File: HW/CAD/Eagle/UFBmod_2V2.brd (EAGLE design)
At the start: 98.4 x 89.5 mm, 204 parts, among them J1411 ABRACON_ARJE-0034, T0551 MMBT2222, U0501 MIDAS_MCCOG21605B6W-FPTLWI, U0601 MAX5217, U0701 AT86RF215-ZU, U0711 ASVTX-13-D-26.000MHZ-I05-T, U0811 PE4259, U0821 RFX1010, U0881 B39871B3440U410, U0911 FT232HL, U1101 TPS53353, U1211 TPS62745DSSR, X0891 ANTENNATINY, X0895 ANTENNATINY, X1011 TTE_EN11-HSM, X1311 MOLEX 105017-0001, X1351 PHOENIX_1990067_1X8X2MM50_PTS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, X1361 PHOENIX_1990067_1X8X2MM50_PTS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

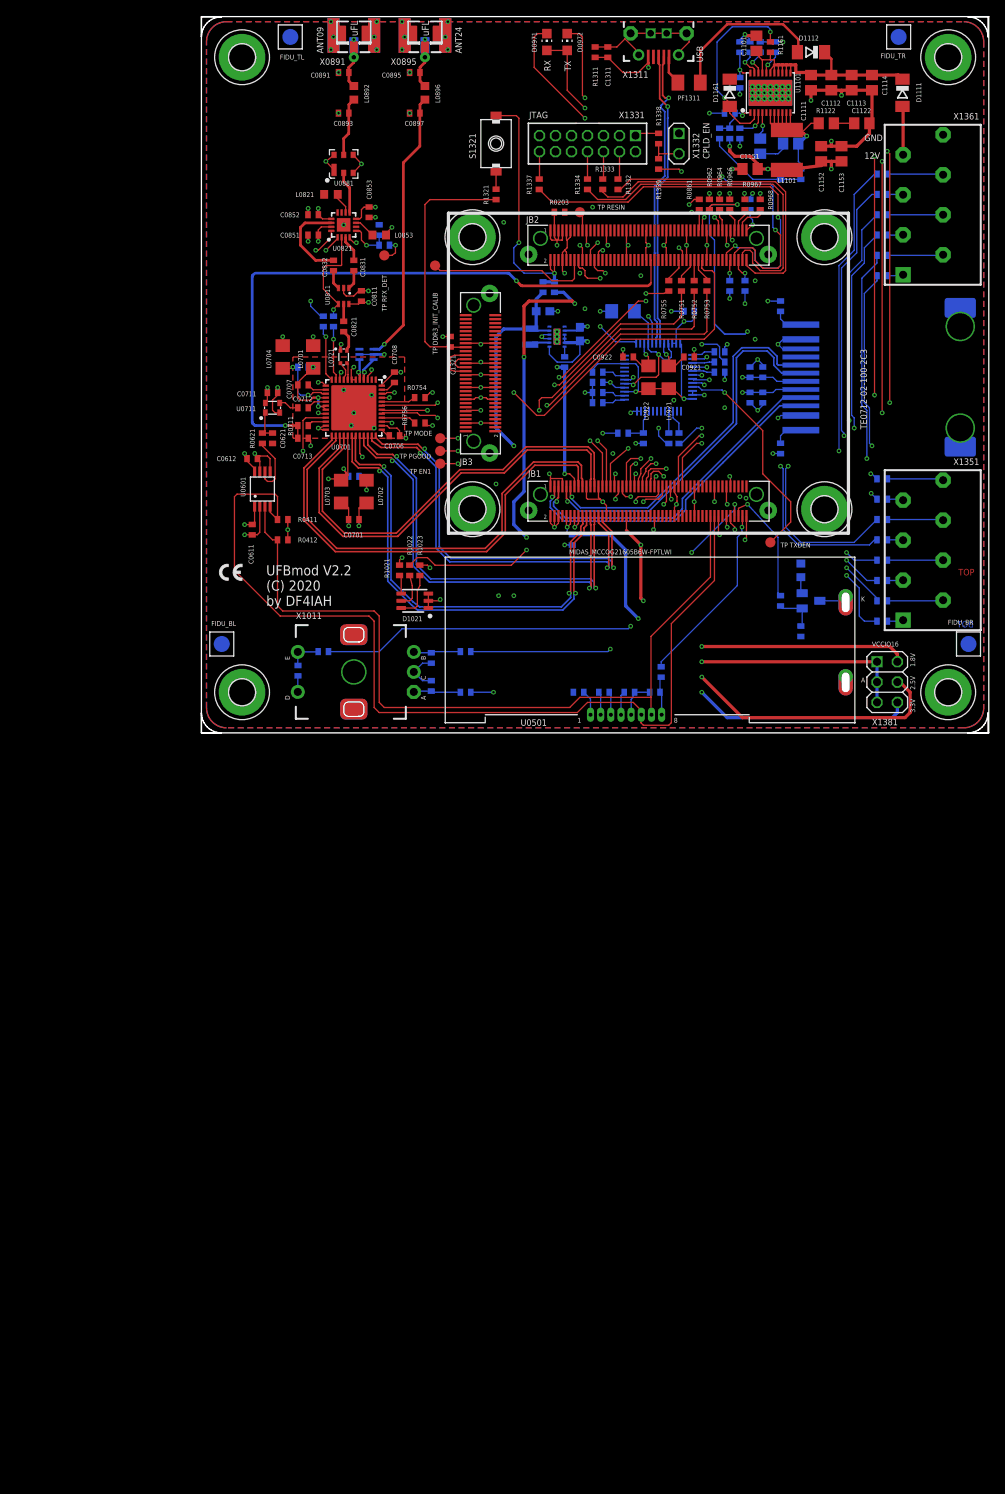
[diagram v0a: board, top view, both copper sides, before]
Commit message: HW - Eagle - V2.2 - FT232H supply fixes, suppressor diodes to be added, layout still to do.
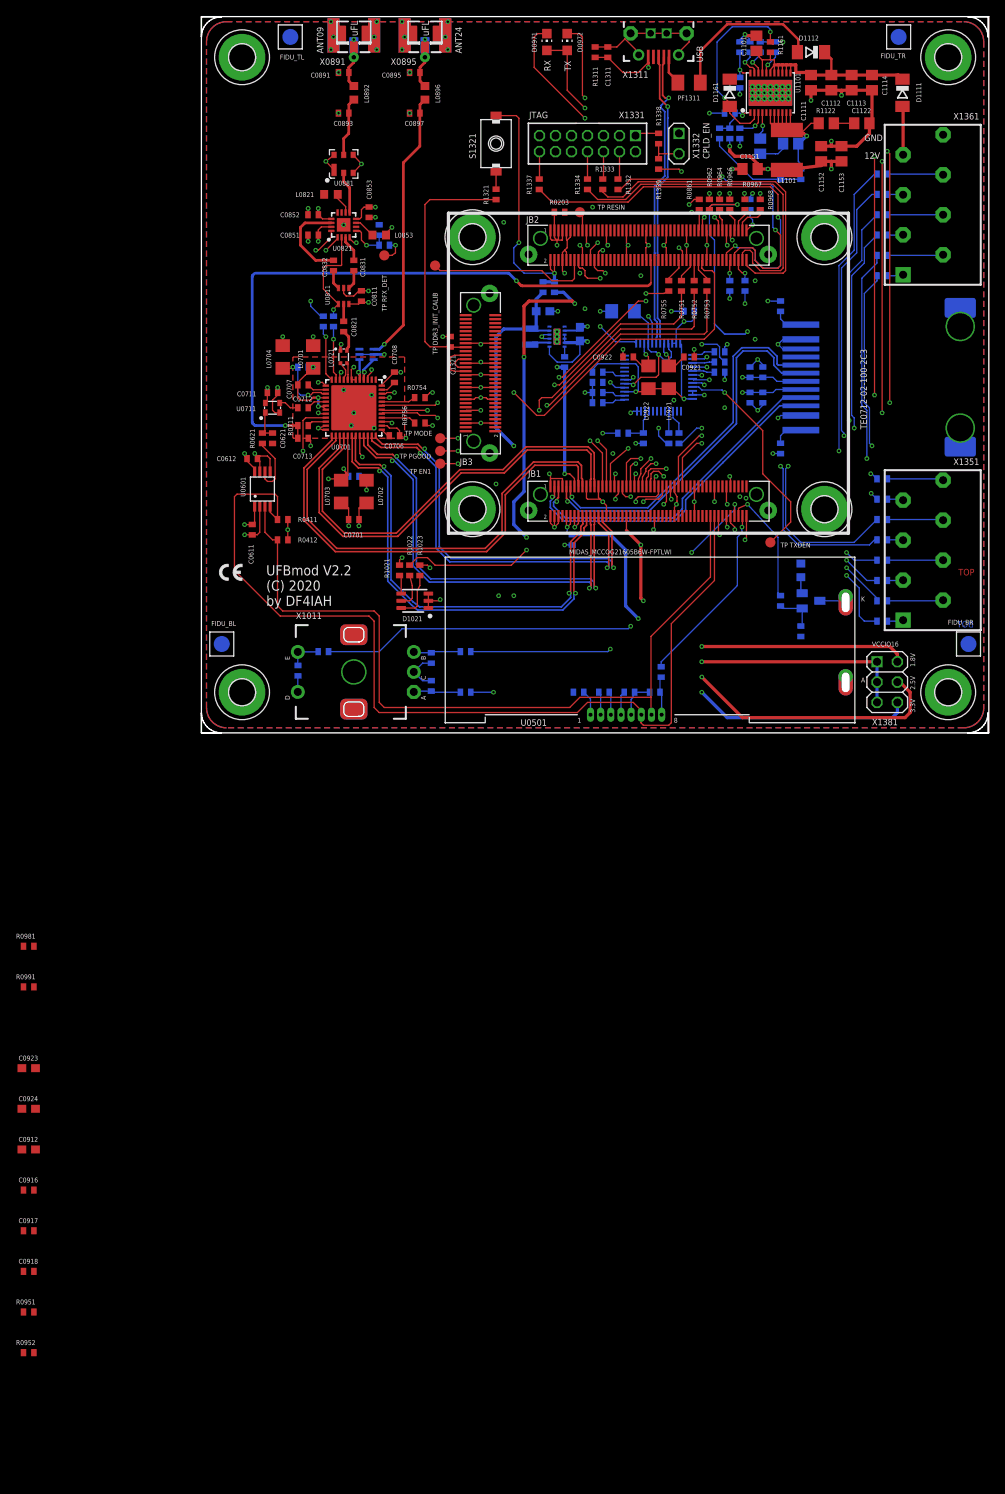
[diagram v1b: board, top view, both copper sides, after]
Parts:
- added C0914, C0916, C0917, C0918: 100nF, df4iah_rcl:C0402
- added C0923, C0924: 4.7uF, df4iah_rcl:C0603
- added R0951, R0952: 0R, df4iah_rcl:R0402
- added R0981: 10kR, df4iah_rcl:R0402
- added R0991: N/A, df4iah_rcl:R0402
- C0912: value 100nF -> 4.7uF; device df4iah_rcl:C0402 -> df4iah_rcl:C0603
- moved C0912 118.4 mm to (-21.6, -52.1), flipped to the top, turned to 0 degrees
- moved C0913 1.27 mm to (49.5, 42.5)
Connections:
- net PMIC3V3_SW renamed PMIC2V5_SW
- removed net FT_VCCCORE: C0912.2, U0911.38
- removed net FT_VCCD: D0971.A, D0972.A, L0921.2, L0922.2, R0931.2, U0911.12, U0911.24, U0911.39, U0911.46
- new net FT_ACBUS7: R0991.2, U0911.31
- new net FT_VCORE: C0913.2, U0911.38
- new net N$1: R0951.2, U0911.6
- new net N$3: R0952.2, U0911.7
- net +3V3: now also C0912.1, C0916.1, C0917.1, C0918.1, D0971.A, D0972.A, L0921.2, L0922.2, R0931.2, R0981.2, U0911.12, U0911.24, U0911.39, U0911.46
- net +5V_USB: now also R0991.1
- net FT_TXDEN: now also R0981.1
- net FT_VCCA: now also C0914.2; no longer C0913.2
- net FT_VPHY: now also C0924.1
- net FT_VPLL: now also C0923.1
- net GND: now also C0912.2, C0914.1, C0916.2, C0917.2, C0918.2, C0923.2, C0924.2; no longer C0912.1
- net USB_D_N: now also R0951.1; no longer U0911.6
- net USB_D_P: now also R0952.1; no longer U0911.7
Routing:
- net FT_VCCD: track 130.4 -> 0.00 mm, vias 5 -> 0
- net +3V3: track 124.7 -> 254.2 mm, vias 22 -> 27
- net FT_VCORE: track 0.00 -> 2.91 mm
- net FT_VCCCORE: track 2.91 -> 0.00 mm
- net USB_D_P: track 36.9 -> 36.1 mm
- net USB_D_N: track 37.7 -> 37.0 mm

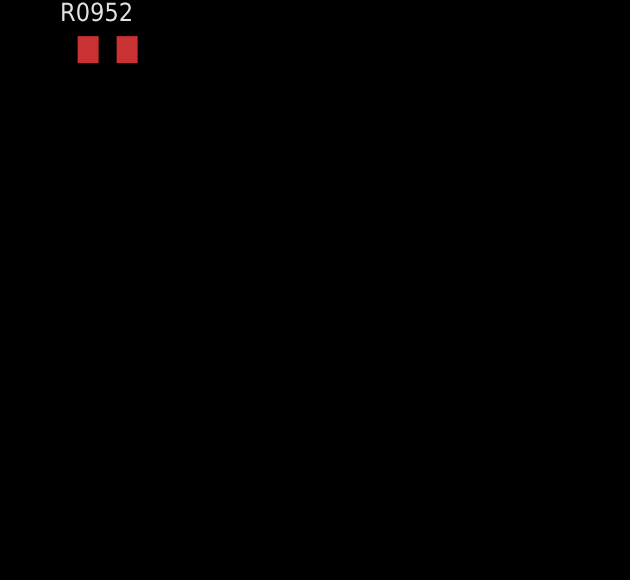
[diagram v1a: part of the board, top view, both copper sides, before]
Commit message: HW - Eagle - V2.2 - font size changed for DAC and volt. reference
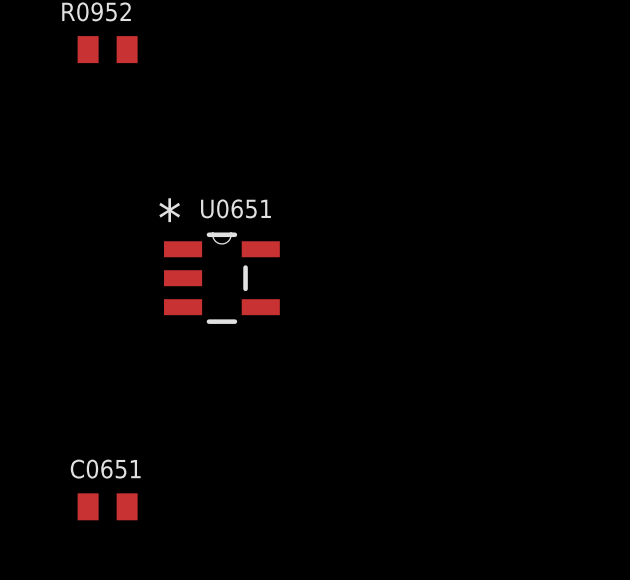
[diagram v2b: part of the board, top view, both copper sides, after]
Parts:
- added C0651: 100nF, df4iah_rcl:C0402
- added U0651: LM4120IM5-3.0, df4iah_powersupply:SOT95P285X120-5N
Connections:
- new net +3V0_20MHZ_VCTCXO: C0611.1, U0601.1, U0651.5
- net +3V3: now also C0651.1, U0651.3, U0651.4; no longer C0611.1, U0601.1
- net GND: now also C0651.2, U0651.2
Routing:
- net +3V3: track 254.2 -> 250.8 mm, vias 27 -> 26
- net +3V0_20MHZ_VCTCXO: track 0.00 -> 3.36 mm, vias 0 -> 1
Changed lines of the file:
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@@
 <element name="R0951" library="df4iah_rcl" package="R0402" value="0R" x="-21.59" y="-72.39"/>
 <element name="R0952" library="df4iah_rcl" package="R0402" value="0R" x="-21.59" y="-77.47"/>
+<element name="U0651" library="df4iah_powersupply" package="SOT95P285X120-5N" value="LM4120IM5-3.0" x="-17.78" y="-85.09">
+<attribute name="OC_FARNELL" value="1312745" x="-17.78" y="-85.09" size="1.778" layer="27" display="off"/>
+<attribute name="MPN" value="LM4120IM5-3.0" x="-17.78" y="-85.09" size="1.778" layer="27" display="off"/>
+<attribute name="OC_NEWARK" value="41K5441" x="-17.78" y="-85.09" size="1.778" layer="27" display="off"/>
+<attribute name="PACKAGE" value="SOT-23-5" x="-17.78" y="-85.09" size="1.778" layer="27" display="off"/>
+<attribute name="SUPPLIER" value="National Semiconductors" x="-17.78" y="-85.09" size="1.778" layer="27" display="off"/>
+</element>
+<element name="C0651" library="df4iah_rcl" package="C0402" value="100nF" x="-21.59" y="-92.71"/>
 </elements>
 <signals>
@@
 <contactref element="C0917" pad="2"/>
 <contactref element="C0918" pad="2"/>
+<contactref element="U0651" pad="2"/>
+<contactref element="C0651" pad="2"/>
 <wire x1="92.71" y1="74.77" x2="93.345" y2="84.455" width="0" layer="19" extent="1-1"/>
 <wire x1="83.82" y1="76.2" x2="92.71" y2="74.77" width="0" layer="19" extent="1-1"/>
@@
 <wire x1="-20.94" y1="-62.23" x2="-20.94" y2="-57.15" width="0" layer="19" extent="1-1"/>
 <wire x1="-20.94" y1="-67.31" x2="-20.94" y2="-62.23" width="0" layer="19" extent="1-1"/>
+<wire x1="-19.0754" y1="-85.09" x2="-20.94" y2="-67.31" width="0" layer="19" extent="1-1"/>
+<wire x1="-20.94" y1="-92.71" x2="-19.0754" y2="-85.09" width="0" layer="19" extent="1-1"/>
 </signal>
 <signal name="+3V3">
@@
 <contactref element="U0821" pad="15"/>
 <contactref element="C0612" pad="1"/>
-<contactref element="C0611" pad="1"/>
-<contactref element="U0601" pad="1"/>
 <wire x1="18.4" y1="26.67" x2="18.4" y2="28.1205" width="0.1524" layer="1"/>
 <wire x1="18.4" y1="28.1205" x2="17.4625" y2="28.7405" width="0.1524" layer="1"/>
@@
 <wire x1="10.795" y1="25.4" x2="10.795" y2="24.145" width="0.1524" layer="1"/>
 <wire x1="10.795" y1="24.145" x2="10.81" y2="24.13" width="0.1524" layer="1"/>
-<via x="5.3975" y="26.035" extent="1-16" drill="0.3"/>
-<wire x1="5.3975" y1="26.035" x2="6.335" y2="26.035" width="0.1524" layer="1"/>
-<wire x1="6.335" y1="26.035" x2="6.35" y2="26.05" width="0.1524" layer="1"/>
-<wire x1="6.645" y1="28.33" x2="6.645" y2="26.345" width="0.1524" layer="1"/>
-<wire x1="6.645" y1="26.345" x2="6.35" y2="26.05" width="0.1524" layer="1"/>
 <wire x1="7.295" y1="32.63" x2="7.3025" y2="32.6375" width="0.1524" layer="1"/>
 <wire x1="7.3025" y1="32.6375" x2="7.3025" y2="33.9725" width="0.1524" layer="1"/>
@@
 <wire x1="71.4375" y1="41.5925" x2="60.4825" y2="41.5925" width="0.1524" layer="3"/>
 <wire x1="60.4825" y1="41.5925" x2="60.325" y2="41.75" width="0.1524" layer="3"/>
+<contactref element="U0651" pad="4"/>
+<contactref element="C0651" pad="1"/>
+<contactref element="U0651" pad="3"/>
 <wire x1="66.04" y1="74.28" x2="67.31" y2="79.8195" width="0" layer="19" extent="16-16"/>
 <wire x1="64.77" y1="72.0725" x2="66.04" y2="72.7075" width="0" layer="19" extent="1-3"/>
@@
 <wire x1="8.255" y1="43.18" x2="10.16" y2="48.412" width="0" layer="19" extent="1-1"/>
 <wire x1="6.6975" y1="34.925" x2="7.99" y2="41.24" width="0" layer="19" extent="1-1"/>
-<wire x1="6.645" y1="28.33" x2="7.295" y2="32.63" width="0" layer="19" extent="1-1"/>
-<wire x1="10.795" y1="26.655" x2="6.645" y2="26.345" width="0" layer="19" extent="1-1"/>
+<wire x1="10.81" y1="26.67" x2="8.595" y2="32.63" width="0" layer="19" extent="1-1"/>
 <wire x1="17.4625" y1="28.7405" x2="10.81" y2="26.67" width="0" layer="19" extent="1-1"/>
 <wire x1="52.84875" y1="5.08" x2="46.6725" y2="25.7175" width="0" layer="19" extent="16-16"/>
 <wire x1="80.53" y1="5.57" x2="52.84875" y2="5.08" width="0" layer="19" extent="1-16"/>
-<wire x1="-20.94" y1="-26.67" x2="5.3975" y2="26.035" width="0" layer="19" extent="1-1"/>
+<wire x1="-20.94" y1="-26.67" x2="10.795" y2="24.145" width="0" layer="19" extent="1-1"/>
 <wire x1="-22.44" y1="-52.07" x2="-20.94" y2="-26.67" width="0" layer="19" extent="1-1"/>
 <wire x1="-22.24" y1="-57.15" x2="-22.44" y2="-52.07" width="0" layer="19" extent="1-1"/>
 <wire x1="-22.24" y1="-62.23" x2="-22.24" y2="-57.15" width="0" layer="19" extent="1-1"/>
 <wire x1="-22.24" y1="-67.31" x2="-22.24" y2="-62.23" width="0" layer="19" extent="1-1"/>
+<wire x1="-19.0754" y1="-86.0552" x2="-22.24" y2="-67.31" width="0" layer="19" extent="1-1"/>
+<wire x1="-16.4846" y1="-86.0552" x2="-19.0754" y2="-86.0552" width="0" layer="19" extent="1-1"/>
+<wire x1="-22.24" y1="-92.71" x2="-19.0754" y2="-86.0552" width="0" layer="19" extent="1-1"/>
 </signal>
 <signal name="P$8">
@@
 <wire x1="-20.94" y1="-77.47" x2="57.35" y2="48.7" width="0" layer="19" extent="1-16"/>
 </signal>
+<signal name="+3V0_20MHZ_VCTCXO">
+<contactref element="U0651" pad="5"/>
+<contactref element="C0611" pad="1"/>
+<contactref element="U0601" pad="1"/>
+<via x="5.3975" y="26.035" extent="1-16" drill="0.3"/>
+<wire x1="5.3975" y1="26.035" x2="6.335" y2="26.035" width="0.1524" layer="1"/>
+<wire x1="6.335" y1="26.035" x2="6.35" y2="26.05" width="0.1524" layer="1"/>
+<wire x1="6.645" y1="28.33" x2="6.645" y2="26.345" width="0.1524" layer="1"/>
+<wire x1="6.645" y1="26.345" x2="6.35" y2="26.05" width="0.1524" layer="1"/>
+<wire x1="5.3975" y1="26.035" x2="-16.4846" y2="-84.1248" width="0" layer="19" extent="1-1"/>
+</signal>
 </signals>

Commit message: HW - Eagle - V2.2 - Ethernet magnetics LED resistor values modified (V2.1 also)
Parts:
- R1421, R1422: value 1kR -> 470R
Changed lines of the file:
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@@
 <attribute name="VALUE" x="85.2932" y="49.6824" size="0.8128" layer="28" font="vector" ratio="20" rot="MR270"/>
 </element>
-<element name="R1421" library="df4iah_rcl" package="R0402" value="1kR" x="72.39" y="35.56" smashed="yes" rot="MR90">
+<element name="R1421" library="df4iah_rcl" package="R0402" value="470R" x="72.39" y="35.56" smashed="yes" rot="MR90">
 <attribute name="NAME" x="73.3425" y="34.29" size="0.6096" layer="26" font="vector" ratio="10" rot="MR90"/>
 <attribute name="VALUE" x="70.8025" y="33.9725" size="0.6096" layer="28" font="vector" ratio="10" rot="MR90"/>
 </element>
-<element name="R1422" library="df4iah_rcl" package="R0402" value="1kR" x="72.39" y="53.34" smashed="yes" rot="MR270">
+<element name="R1422" library="df4iah_rcl" package="R0402" value="470R" x="72.39" y="53.34" smashed="yes" rot="MR270">
 <attribute name="NAME" x="72.0725" y="54.9275" size="0.6096" layer="26" font="vector" ratio="10" rot="MR90"/>
 <attribute name="VALUE" x="73.9775" y="54.9275" size="0.6096" layer="28" font="vector" ratio="10" rot="MR270"/>

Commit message: HW - Eagle - V2.1 V2.2 - TRX corrections added
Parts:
- C0703, C0704: value 1nF -> 1uF
- C0713: value 1nF -> N/A
- R0711: value 33R -> 130R
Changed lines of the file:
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@@
 <attribute name="VALUE" x="7.62" y="48.26" size="1.27" layer="27" rot="R270"/>
 </element>
-<element name="C0704" library="df4iah_rcl" package="C0402" value="1nF" x="12.7" y="45.72" smashed="yes" rot="MR180">
+<element name="C0704" library="df4iah_rcl" package="C0402" value="1uF" x="12.7" y="45.72" smashed="yes" rot="MR180">
 <attribute name="NAME" x="13.97" y="46.6725" size="0.6096" layer="26" font="vector" ratio="10" rot="MR0"/>
 <attribute name="VALUE" x="11.43" y="47.3075" size="0.6096" layer="28" font="vector" ratio="10" rot="MR180"/>
 </element>
-<element name="C0703" library="df4iah_rcl" package="C0402" value="1nF" x="19.05" y="32.0675" smashed="yes" rot="MR180">
+<element name="C0703" library="df4iah_rcl" package="C0402" value="1uF" x="19.05" y="32.0675" smashed="yes" rot="MR180">
 <attribute name="NAME" x="21.2725" y="33.02" size="0.6096" layer="26" font="vector" ratio="10" rot="MR0"/>
 <attribute name="VALUE" x="17.78" y="33.655" size="0.6096" layer="28" font="vector" ratio="10" rot="MR180"/>
@@
 <attribute name="VALUE" x="38.4175" y="65.7225" size="0.6096" layer="27" font="vector" ratio="10" rot="R90"/>
 </element>
-<element name="R0711" library="df4iah_rcl" package="R0402" value="33R" x="12.7" y="38.4175" smashed="yes">
+<element name="R0711" library="df4iah_rcl" package="R0402" value="130R" x="12.7" y="38.4175" smashed="yes">
 <attribute name="NAME" x="11.43" y="37.1475" size="0.6096" layer="25" font="vector" ratio="10" rot="R90"/>
 <attribute name="VALUE" x="11.1125" y="36.83" size="0.6096" layer="27" font="vector" ratio="10"/>
@@
 <attribute name="VALUE" x="29.5275" y="50.165" size="0.6096" layer="27" font="vector" ratio="10" rot="R270"/>
 </element>
-<element name="C0713" library="df4iah_rcl" package="C0402" value="1nF" x="12.7" y="36.83" smashed="yes" rot="R180">
+<element name="C0713" library="df4iah_rcl" package="C0402" value="N/A" x="12.7" y="36.83" smashed="yes" rot="R180">
 <attribute name="NAME" x="11.43" y="34.29" size="0.6096" layer="25" font="vector" ratio="10"/>
 <attribute name="VALUE" x="13.97" y="38.4175" size="0.6096" layer="27" font="vector" ratio="10" rot="R180"/>

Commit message: HW - Eagle - V2.1 V2.2 - TRX no 300R inductors at GND lines
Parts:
- removed L0701, L0702: 300R, df4iah_rcl:R1206
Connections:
- removed net TRX_AVSS: C0704.2, C0707.1, C0708.1, L0701.2, U0701.10, U0701.16, U0701.18, U0701.19, U0701.3, U0701.45, U0701.48, U0701.49, U0701.6, U0701.7
- removed net TRX_DVSS: C0703.2, C0706.1, L0702.2, U0701.20, U0701.23, U0701.24, U0701.32, U0701.38
- net GND: now also C0703.2, C0704.2, C0706.1, C0707.1, C0708.1, U0701.10, U0701.16, U0701.18, U0701.19, U0701.20, U0701.23, U0701.24, U0701.3, U0701.32, U0701.38, U0701.45, U0701.48, U0701.49, U0701.6, U0701.7; no longer L0701.1, L0702.1
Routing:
- net GND: track 242.1 -> 307.5 mm, vias 84 -> 101
- net TRX_DVSS: track 37.0 -> 0.00 mm, vias 5 -> 0
- net TRX_AVSS: track 33.0 -> 0.00 mm, vias 13 -> 0

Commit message: HW - Eagle - V2.1 V2.2 - PMIC values changed for lower swing at VFB and OV-protection
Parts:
- R1103: value 187kR -> N/A
- R1131: value 3.01kR -> 15kR
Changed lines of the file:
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@@
 <attribute name="VALUE" x="78.105" y="80.01" size="0.6096" layer="27" font="vector" ratio="10" rot="R90"/>
 </element>
-<element name="R1103" library="df4iah_rcl" package="R0402" value="187kR" x="67.31" y="85.725" smashed="yes" rot="MR270">
+<element name="R1103" library="df4iah_rcl" package="R0402" value="N/A" x="67.31" y="85.725" smashed="yes" rot="MR270">
 <attribute name="NAME" x="65.7225" y="84.455" size="0.6096" layer="26" font="vector" ratio="10" rot="MR90"/>
 <attribute name="VALUE" x="68.8975" y="87.3125" size="0.6096" layer="28" font="vector" ratio="10" rot="MR270"/>
@@
 <attribute name="VALUE" x="81.28" y="74.295" size="0.6096" layer="27" font="vector" ratio="10"/>
 </element>
-<element name="R1131" library="df4iah_rcl" package="R0402" value="3.01kR" x="74.93" y="69.85" smashed="yes" rot="MR270">
+<element name="R1131" library="df4iah_rcl" package="R0402" value="15kR" x="74.93" y="69.85" smashed="yes" rot="MR270">
 <attribute name="NAME" x="75.8825" y="68.58" size="0.6096" layer="26" font="vector" ratio="10" rot="MR90"/>
 <attribute name="VALUE" x="76.5175" y="71.4375" size="0.6096" layer="28" font="vector" ratio="10" rot="MR270"/>
